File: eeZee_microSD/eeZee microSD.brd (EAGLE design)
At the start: 20.2 x 29.2 mm, 12 parts, among them U1 MCP1824S

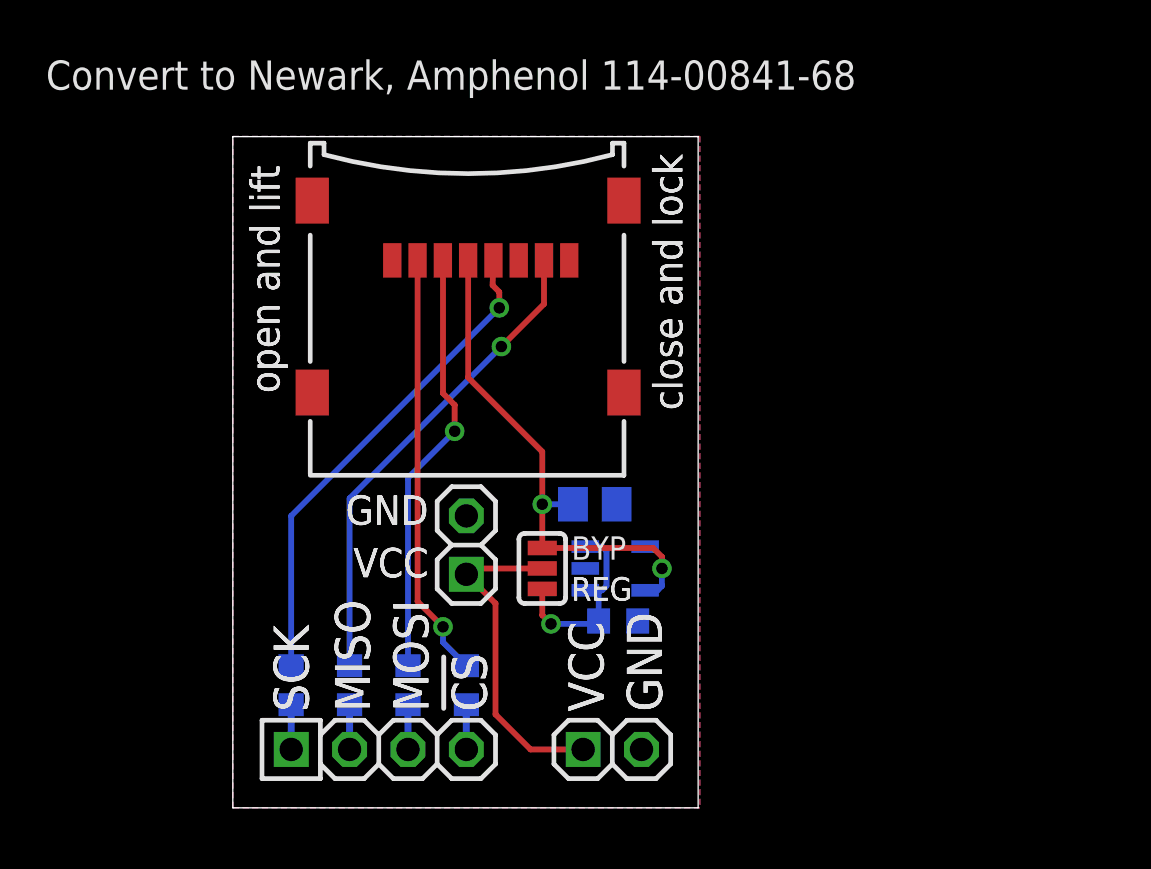
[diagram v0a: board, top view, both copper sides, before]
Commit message: Added offset power strip header, tweaked layout, optimized 74HC4050 pin use, etc.
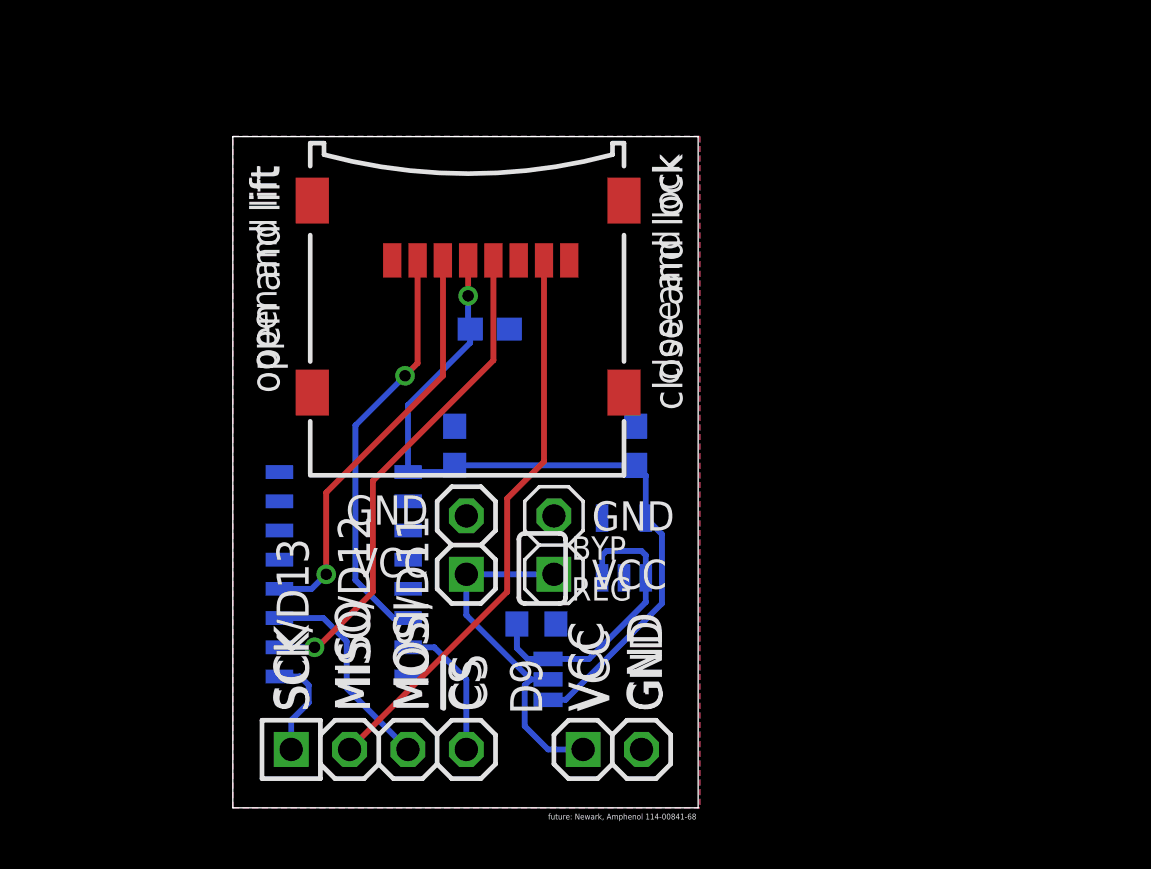
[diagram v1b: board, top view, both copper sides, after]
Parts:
- removed R1, R2, R3, R4: 1k, rcl:R0603
- added C2, C3: 0.1uF, rcl:C0603
- added JP5: (no value), pinhead-2:1X04-S
- added U2: 74HC4050, SparkFun:SO016
- C1: device rcl:C0805 -> rcl:C0603
- JP2: device pinhead-2:1X04-S -> pinhead-2:1X02-S
- U1: device SparkFun:SOT23-5 -> mes_regulators:SOT23-5
- moved JP2 9.67 mm to (10.2, 11.4), turned to 90 degrees
- moved REG 4.83 mm to (13.7, 5.59), flipped to the bottom, turned to 90 degrees
- moved JP3 3.81 mm to (14.0, 11.4)
- moved R5 3.56 mm to (13.2, 8.00)
- moved C1 3.10 mm to (17.5, 15.7), turned to 90 degrees
- moved U1 0.97 mm to (17.0, 11.3), turned to 0 degrees
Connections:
- removed net !SS_HV: JP2.4, R3.2
- removed net MISO_HV: JP2.2, R1.2
- removed net N$2: JP2.3, R4.2
- new net !CS_HV: JP5.4, U2.7
- new net MOSI_HV: JP5.3, U2.11
- net !SS: now also U2.6; no longer R3.1
- net GND: now also C2.2, C3.2, JP2.2, U2.14, U2.3, U2.5, U2.8
- net MISO: now also JP5.2; no longer R1.1
- net MOSI: now also U2.12; no longer R4.1
- net SCK: now also U2.10; no longer R2.1
- net SCK_HV: now also JP5.1, U2.9; no longer JP2.1, R2.2
- net VCC: now also JP2.1
- net VOUT: now also C2.1, C3.1, U2.1
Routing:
- net VOUT: track 22.6 -> 33.4 mm, vias 2 -> 1
- net MOSI_HV: track 0.00 -> 9.15 mm
- net !CS_HV: track 0.00 -> 6.16 mm
- net VIN: track 8.70 -> 13.0 mm, vias 1 -> 0
- net MISO: track 21.1 -> 24.8 mm, vias 1 -> 0
- net SCK_HV: track 1.94 -> 4.54 mm
- net N$2: track 1.94 -> 0.00 mm
- net MISO_HV: track 1.94 -> 0.00 mm
- net !SS_HV: track 1.94 -> 0.00 mm
- net VCC: track 14.5 -> 15.4 mm
- net MOSI: track 18.7 -> 18.1 mm
- net !SS: track 18.5 -> 18.0 mm
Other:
- board text added: "D9"
- board text added: "MISO/D12"
- board text added: "MOSI/D11"
- board text added: "SCK/D13"
- board text added: "future: Newark, Amphenol 114-00841-68"
- board text removed: "Convert to Newark, Amphenol 114-00841-68"
